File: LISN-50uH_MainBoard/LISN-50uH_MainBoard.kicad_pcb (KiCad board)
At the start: 2 copper layers, 100 x 100 mm, 76 parts, among them J1 Conn_Coaxial, J2 Conn_Coaxial, J3 Conn_01x01_Pin, J4 Conn_01x01_Pin, J5 Conn_01x01_Pin, J6 Conn_01x01_Pin

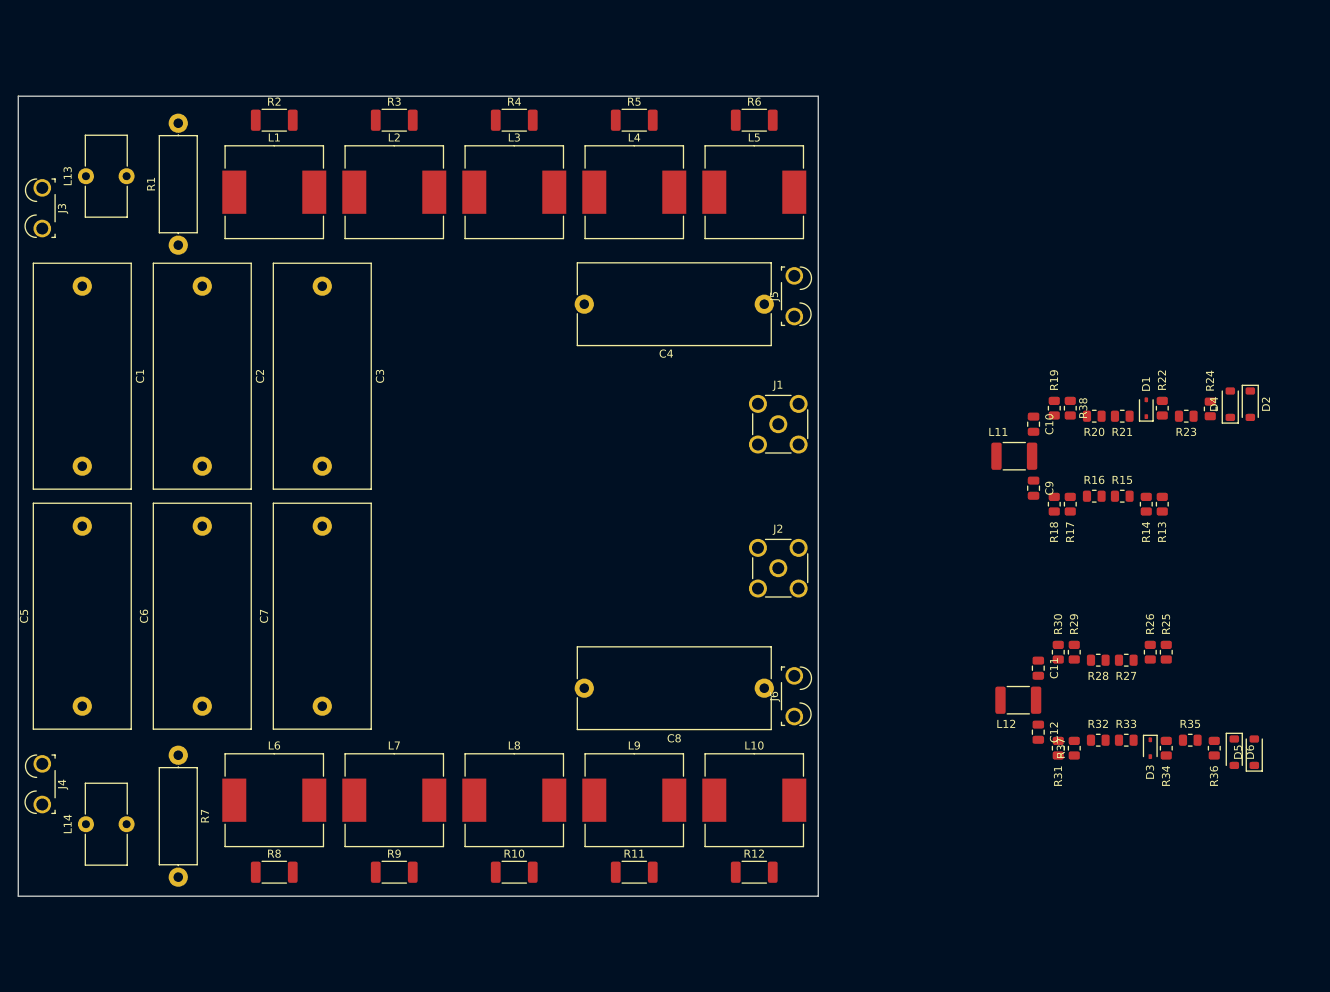
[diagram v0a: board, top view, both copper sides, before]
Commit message: sch update - changes in filter path. pcb - change PCB dimensions
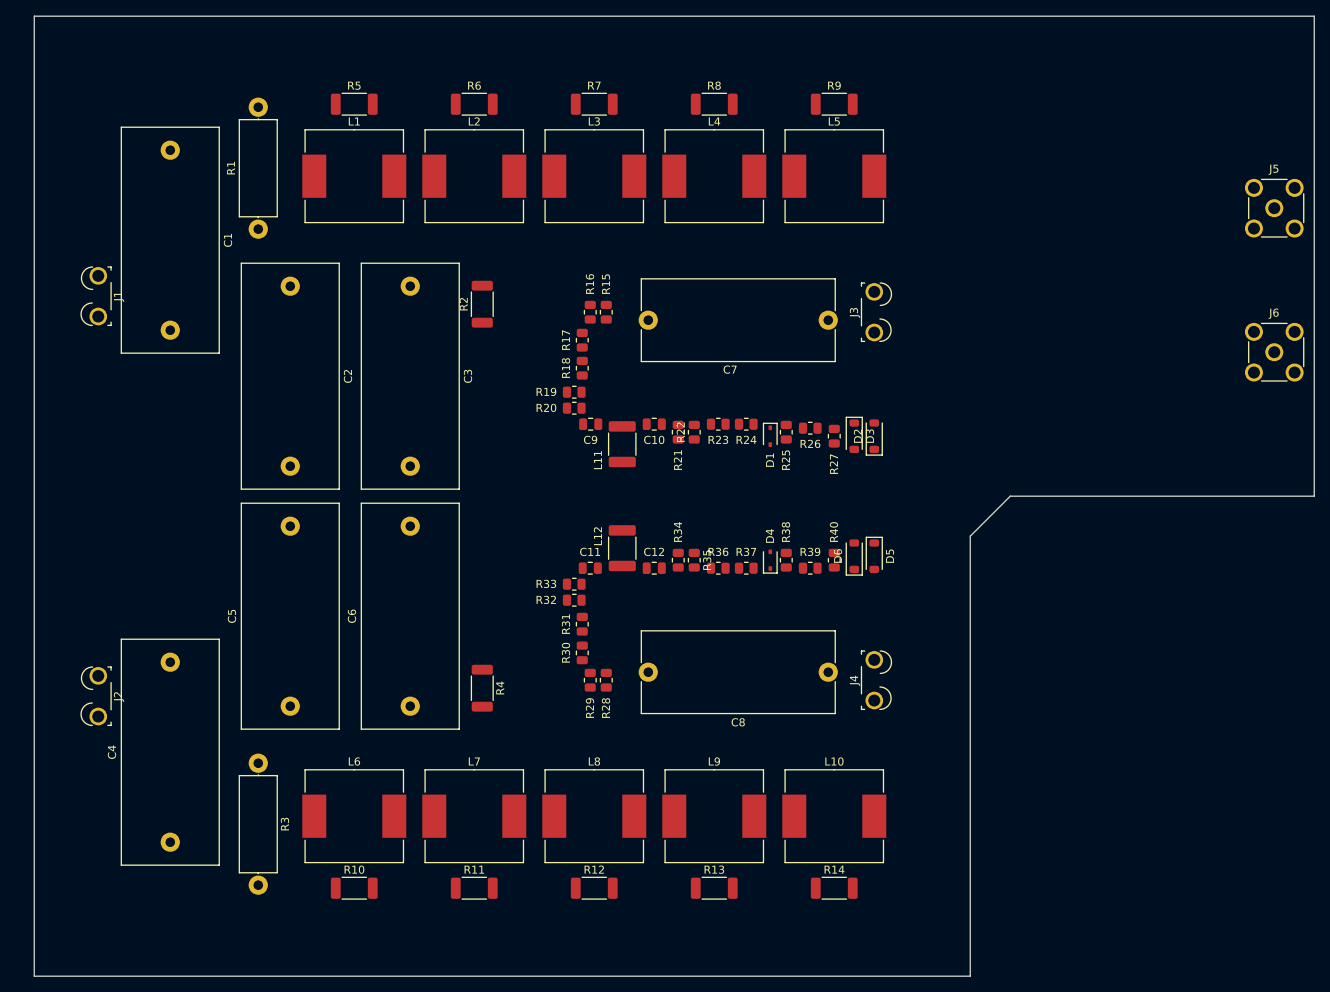
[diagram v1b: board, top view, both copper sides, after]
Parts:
- removed L13, L14: L, Inductor_THT:L_Toroid_Vertical_L10.0mm_W5.0mm_P5.08mm
- added R2: R, Resistor_SMD:R_2010_5025Metric, F.Cu at (126.0, 76.0)
- added R4: R, Resistor_SMD:R_2010_5025Metric, F.Cu at (126.0, 124.0)
- moved R15 73.5 mm to (141.5, 77.0), turned to -90 degrees
- moved R16 73.5 mm to (139.5, 77.0), turned to -90 degrees
- moved R17 70.3 mm to (138.5, 80.5), turned to -90 degrees
- moved R28 70.1 mm to (141.5, 123.0), turned to 90 degrees
- moved R29 70.1 mm to (139.5, 123.0), turned to 90 degrees
- moved R30 68.0 mm to (138.5, 119.6), turned to 90 degrees
- moved J5 67.6 mm to (225.0, 64.0)
- moved J6 67.6 mm to (225.0, 82.0)
- moved R18 66.0 mm to (138.5, 84.0), turned to -90 degrees
- moved R31 64.7 mm to (138.5, 116.0), turned to 90 degrees
- moved R19 63.6 mm to (137.5, 87.0), turned to 0 degrees
- moved R32 62.8 mm to (137.5, 113.0), turned to 0 degrees
- moved R20 61.2 mm to (137.5, 89.0), turned to 0 degrees
- moved R33 61.1 mm to (137.5, 111.0), turned to 0 degrees
- moved C11 57.4 mm to (139.5, 109.0), turned to 0 degrees
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- renumbered C5 to C4, C6 to C5, C7 to C6, C4 to C7, D4 to D3, D3 to D4, J3 to J1, J4 to J2, J5 to J3, J6 to J4, J1 to J5, J2 to J6, R8 to R10, R9 to R11, R10 to R12, R11 to R13, R12 to R14, R13 to R15, R14 to R16, R15 to R17, R16 to R18, R17 to R19, R18 to R20, R19 to R21, R38 to R22, R20 to R23, R21 to R24, R22 to R25, R23 to R26, R24 to R27, R25 to R28, R26 to R29, R7 to R3, R27 to R30, R28 to R31, R29 to R32, R30 to R33, R31 to R34, R37 to R35, R32 to R36, R33 to R37, R34 to R38, R35 to R39, R36 to R40, R2 to R5, R3 to R6, R4 to R7, R5 to R8, R6 to R9
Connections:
- net L_det renamed L_SIG
- net N_det renamed N_SIG
- net Net-(D2-A) renamed L_SIG_LIM
- net Net-(D5-A) renamed N_SIG_LIM
- J1 pad 1: Net-(J3-Pin_1) (its old number) -> Net-(J1-Pin_1)
- J2 pad 1: Net-(J4-Pin_1) (its old number) -> Net-(J2-Pin_1)
- L1 pad 1: Net-(L1-Pad1) -> Net-(J1-Pin_1)
- L6 pad 1: Net-(L14-Pad2) -> Net-(J2-Pin_1)
- R1 pad 2: Net-(L1-Pad1) -> Net-(J1-Pin_1)
- R10 pad 1: Net-(L14-Pad2) -> Net-(J2-Pin_1)
- R3 pad 2: Net-(L14-Pad2) -> Net-(J2-Pin_1)
- R5 pad 1: Net-(L1-Pad1) -> Net-(J1-Pin_1)
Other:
- board size 100 x 100 mm -> 160 x 120 mm

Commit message: changes in low pass filter/limiter path
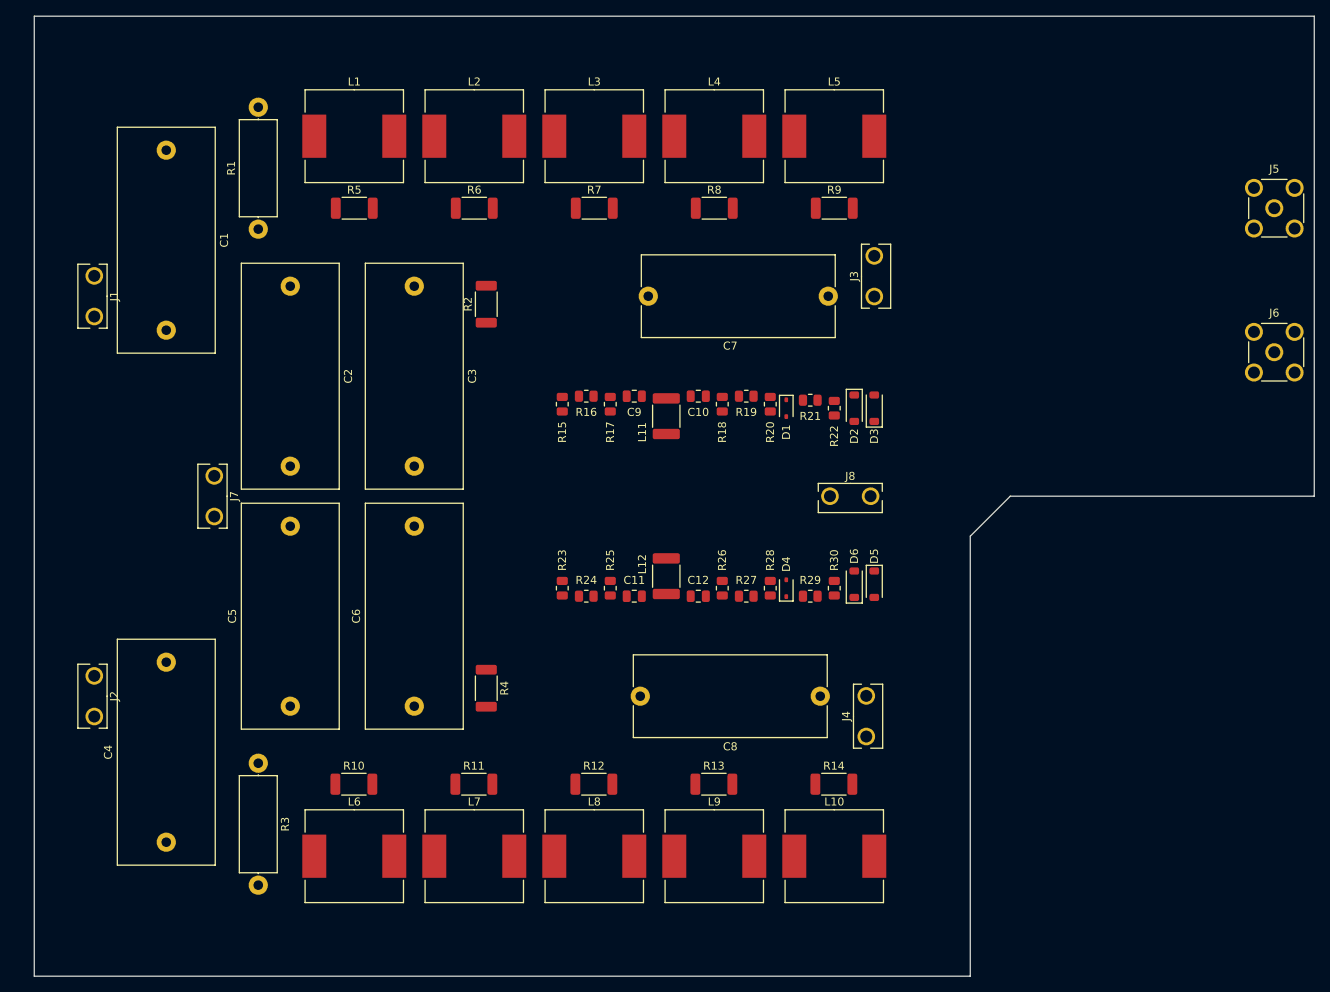
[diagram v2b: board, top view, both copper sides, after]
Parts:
- removed the R16 at (139.5, 77.0)
- removed the R18 at (138.5, 84.0)
- removed the R20 at (137.5, 89.0)
- removed the R22 at (152.5, 92.0)
- removed the R24 at (159.0, 91.0)
- removed the R29 at (139.5, 123.0)
- removed R31: 7R5, Resistor_SMD:R_0805_2012Metric
- removed R33: 430R, Resistor_SMD:R_0805_2012Metric
- removed R35: 220R, Resistor_SMD:R_0805_2012Metric
- removed R37: 15R, Resistor_SMD:R_0805_2012Metric
- added J7: Conn_01x01_Pin, a_project_library:Faston_Tab_6.3x0.8, F.Cu at (92.5, 100.0)
- added J8: Conn_01x01_Pin, a_project_library:Faston_Tab_6.3x0.8, F.Cu at (172.0, 100.0)
- R15: value 620R -> 294R
- R16: renamed from R17; value 10R -> 17R4
- R17: renamed from R19; value 430R -> 215R
- R18: renamed from R21; value 220R -> 110R
- R19: renamed from R23; value 15R -> 30R
- R23: renamed from R28; value 620R -> 294R
- R24: renamed from R30; value 10R -> 17R4
- R25: renamed from R32; value 430R -> 215R
- R26: renamed from R34; value 220R -> 110R
- R27: renamed from R36; value 15R -> 30R
- moved R10 13.0 mm to (110.0, 136.0)
- moved R11 13.0 mm to (125.0, 136.0)
- moved R12 13.0 mm to (139.9, 136.0)
- moved R13 13.0 mm to (154.9, 136.0)
- moved R14 13.0 mm to (169.9, 136.0)
- moved R5 13.0 mm to (110.0, 64.0)
- moved R6 13.0 mm to (125.0, 64.0)
- moved R7 13.0 mm to (140.0, 64.0)
- moved R8 13.0 mm to (155.0, 64.0)
- moved R9 13.0 mm to (170.0, 64.0)
- moved R15 12.7 mm to (136.0, 88.5), turned to 90 degrees
- moved R23 12.7 mm to (136.0, 111.5), turned to -90 degrees
- moved R24 7.11 mm to (139.0, 112.5), turned to 0 degrees
- moved R16 7.02 mm to (139.0, 87.5), turned to 0 degrees
- moved C10 6.52 mm to (153.0, 87.5)
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- renumbered R25 to R20, R26 to R21, R27 to R22, R38 to R28, R39 to R29, R40 to R30
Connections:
- R16 pad 2: Net-(R17-Pad2) -> Net-(C9-Pad1)
- R19 pad 1: Net-(R23-Pad1) -> Net-(D1-A1)
- R24 pad 2: Net-(R30-Pad2) -> Net-(C11-Pad1)
- R27 pad 1: Net-(R36-Pad1) -> Net-(D4-A1)

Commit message: sch - add GDT and optional input toroidal line choke pcb - routing in progress
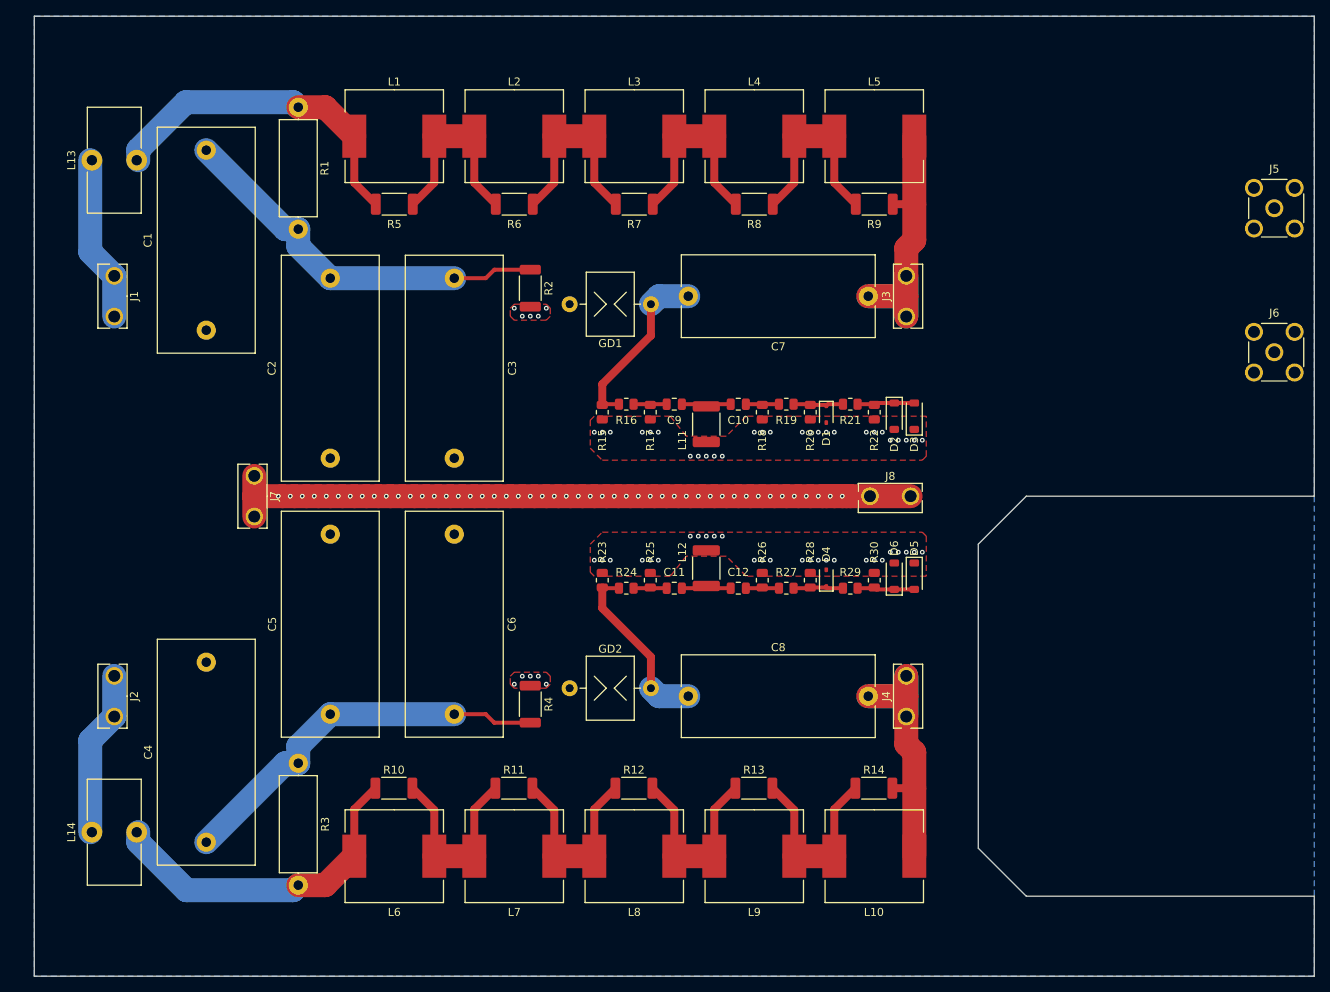
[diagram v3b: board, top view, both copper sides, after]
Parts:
- added GD1: GDT_2Pin, a_project_library:GDT_D8_P10.16_Horizontal, F.Cu at (142.0, 76.0)
- added GD2: GDT_2Pin, a_project_library:GDT_D8_P10.16_Horizontal, F.Cu at (142.0, 124.0)
- added L13: L, Inductor_THT:L_Toroid_Vertical_L13.0mm_W6.5mm_P5.60mm, F.Cu at (77.2, 58.0)
- added L14: L, Inductor_THT:L_Toroid_Vertical_L13.0mm_W6.5mm_P5.60mm, F.Cu at (77.2, 142.0)
- J1, J2, J3, J4, J7, J8: value Conn_01x01_Pin -> Faston Tab 6.3mm
- moved C8 6.00 mm to (174.2, 125.0)
- moved R2 5.85 mm to (132.0, 74.0)
- moved R4 5.85 mm to (132.0, 126.0)
- moved J4 5.59 mm to (179.0, 125.0)
- moved D4 5.15 mm to (169.0, 110.2)
- moved C10 5.10 mm to (158.0, 88.5)
- moved C11 5.10 mm to (150.0, 111.5)
- moved C12 5.10 mm to (158.0, 111.5)
- moved C2 5.10 mm to (107.0, 72.8)
- moved C3 5.10 mm to (122.5, 72.8)
- moved C5 5.10 mm to (107.0, 127.2)
- moved C6 5.10 mm to (122.5, 127.2)
- moved C9 5.10 mm to (150.0, 88.5)
- moved D2 5.10 mm to (180.0, 90.0)
- moved D3 5.10 mm to (177.5, 90.0)
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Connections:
- net Net-(C1-Pad1) renamed /L_C
- net Net-(C4-Pad1) renamed /N_C
- net Net-(J3-Pin_1) renamed /L_dut
- net Net-(J4-Pin_1) renamed /N_dut
- net Net-(L1-Pad2) renamed /L_l1
- net Net-(L10-Pad1) renamed /N_l4
- net Net-(L2-Pad2) renamed /L_l2
- net Net-(L3-Pad2) renamed /L_l3
- net Net-(L4-Pad2) renamed /L_l4
- net Net-(L6-Pad2) renamed /N_l1
- net Net-(L7-Pad2) renamed /N_l2
- net Net-(L8-Pad2) renamed /N_l3
- J1 pad 1: Net-(J1-Pin_1) -> /L_in
- J2 pad 1: Net-(J2-Pin_1) -> /N_in
- L1 pad 1: Net-(J1-Pin_1) -> /L_l
- L6 pad 1: Net-(J2-Pin_1) -> /N_l
- R1 pad 2: Net-(J1-Pin_1) -> /L_l
- R10 pad 1: Net-(J2-Pin_1) -> /N_l
- R3 pad 2: Net-(J2-Pin_1) -> /N_l
- R5 pad 1: Net-(J1-Pin_1) -> /L_l
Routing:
- net GND: track 0.00 -> 87.1 mm, vias 0 -> 112
- net /N_C: track 0.00 -> 48.8 mm
- net /L_C: track 0.00 -> 48.8 mm
- net /L_l: track 0.00 -> 42.1 mm
- net /N_l: track 0.00 -> 42.1 mm
- net /N_dut: track 0.00 -> 40.3 mm
- net /L_dut: track 0.00 -> 40.2 mm
- net /N_l4: track 0.00 -> 24.2 mm
- net /N_l3: track 0.00 -> 24.2 mm
- net /N_l2: track 0.00 -> 24.2 mm
- net /L_l4: track 0.00 -> 24.2 mm
- net /L_l3: track 0.00 -> 24.2 mm
- net /L_l2: track 0.00 -> 24.2 mm
- net /L_l1: track 0.00 -> 24.2 mm
- net /N_l1: track 0.00 -> 24.2 mm
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- added copper zone on B.Cu, net GND
- added copper zone on F.Cu, net GND
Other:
- outline, holes or cut-outs redrawn

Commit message: change input coil footprint, add RF transformer for CM/DM
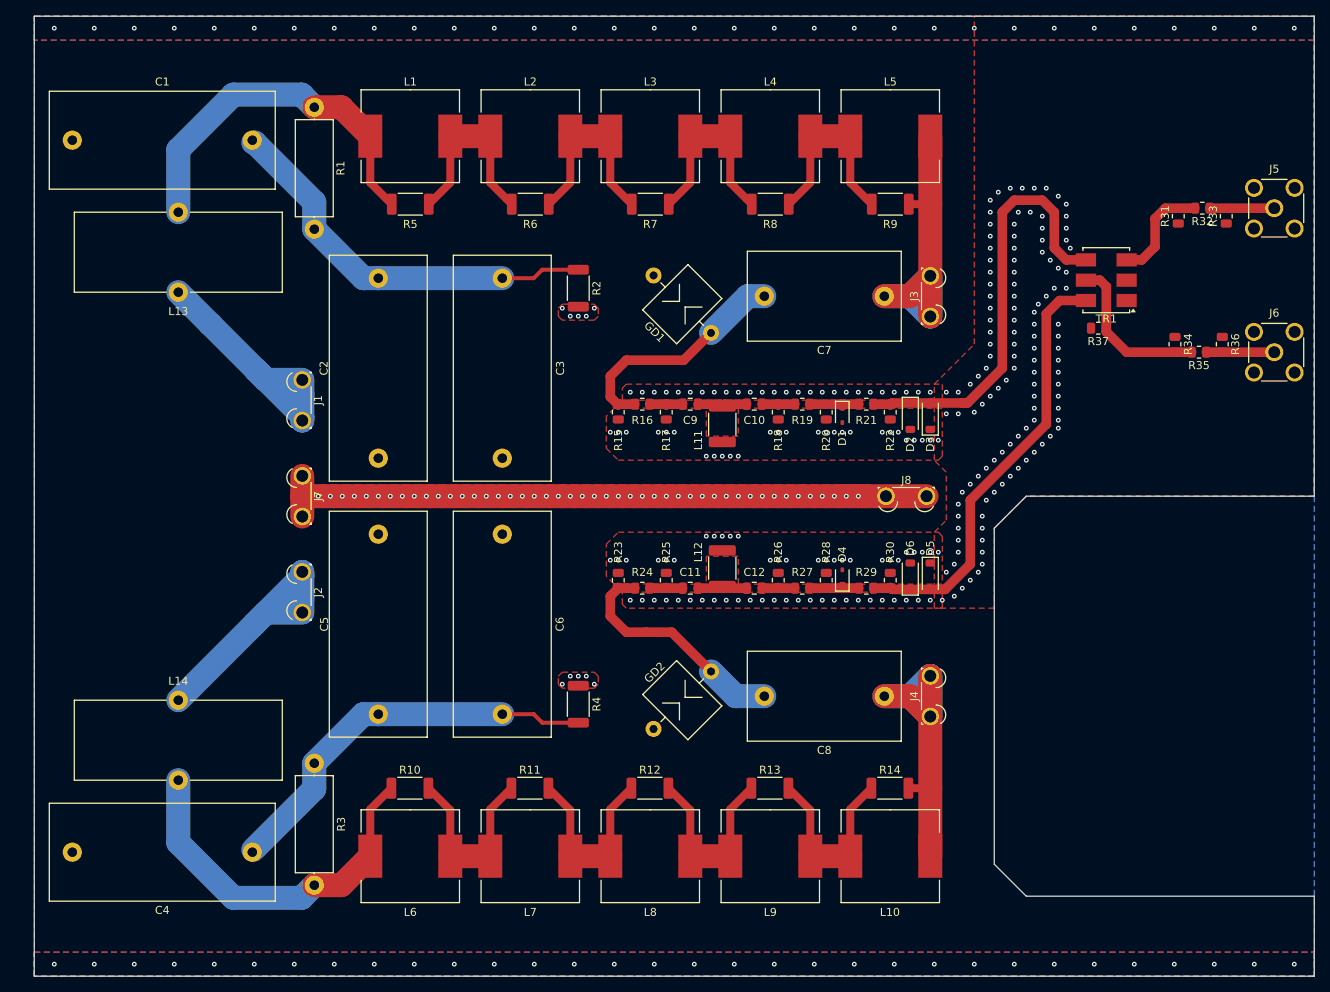
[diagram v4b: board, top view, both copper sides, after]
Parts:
- added R31: DNP, Resistor_SMD:R_0805_2012Metric, F.Cu at (213.0, 65.0)
- added R32: 0, Resistor_SMD:R_0805_2012Metric, F.Cu at (216.0, 64.0)
- added R33: DNP, Resistor_SMD:R_0805_2012Metric, F.Cu at (219.0, 65.0)
- added R34: DNP, Resistor_SMD:R_0805_2012Metric, F.Cu at (212.6, 81.0)
- added R35: 0R, Resistor_SMD:R_0805_2012Metric, F.Cu at (215.6, 82.0)
- added R36: DNP, Resistor_SMD:R_0805_2012Metric, F.Cu at (218.5, 81.0)
- added R37: 50R, Resistor_SMD:R_0805_2012Metric, F.Cu at (203.0, 79.0)
- added TR1: ADT1-6T, RF_Mini-Circuits:Mini-Circuits_CD637_H5.23mm, F.Cu at (204.0, 73.0)
- C7, C8: footprint Capacitor_THT:C_Rect_L24.0mm_W10.1mm_P22.50mm_MKT -> Capacitor_THT:C_Rect_L19.0mm_W11.0mm_P15.00mm_MKS4
- J1, J2, J3, J4, J7, J8: value Faston Tab 6.3mm -> Faston Tab 4.8mm; footprint a_project_library:Faston_Tab_6.3x0.8 -> a_project_library:Faston_Tab_4.8x0.8
- L13, L14: value L -> 250uH optional; footprint Inductor_THT:L_Toroid_Vertical_L13.0mm_W6.5mm_P5.60mm -> a_project_library:L_Toroid_Vertical_L26.0mm_W12.9mm_P10.0mm_Wuerth_WE-FI
- moved J1 26.9 mm to (103.5, 88.0)
- moved J2 26.9 mm to (103.5, 112.0)
- moved L13 15.8 mm to (88.0, 69.5), turned to 180 degrees
- moved L14 15.8 mm to (88.0, 130.5), turned to 0 degrees
- moved GD2 9.12 mm to (151.0, 125.5), turned to 45 degrees
- moved GD1 9.00 mm to (151.0, 76.0), turned to -45 degrees
- moved C2 6.00 mm to (113.0, 72.8)
- moved C3 6.00 mm to (128.5, 72.8)
- moved C5 6.00 mm to (113.0, 127.2)
- moved C6 6.00 mm to (128.5, 127.2)
- moved J7 6.00 mm to (103.5, 100.0)
- moved R2 6.00 mm to (138.0, 74.0)
- moved R4 6.00 mm to (138.0, 126.0)
- moved C1 5.88 mm to (97.2, 55.5), turned to 180 degrees
- moved C4 5.88 mm to (97.2, 144.5), turned to 180 degrees
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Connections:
- J5 pad 1: unconnected-(J5-In-Pad1) -> /SIG_DM_out
- J5 pad 2: unconnected-(J5-Ext-Pad2) -> GND
- J6 pad 1: unconnected-(J6-In-Pad1) -> /SIG_CM_out
- J6 pad 2: unconnected-(J6-Ext-Pad2) -> GND
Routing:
- net N_SIG_LIM: track 7.22 -> 54.4 mm
- net L_SIG_LIM: track 7.22 -> 54.3 mm
- net /SIG_CM: track 0.00 -> 20.3 mm
- net /L_in: track 20.8 -> 34.8 mm
- net /N_in: track 20.8 -> 34.6 mm
- net /SIG_DM: track 0.00 -> 13.3 mm
- net /N_dut: track 40.3 -> 49.1 mm
- net /L_dut: track 40.2 -> 49.0 mm
- net /SIG_CM_out: track 0.00 -> 8.50 mm
- net /SIG_DM_out: track 0.00 -> 8.09 mm
- net N_SIG: track 22.3 -> 29.5 mm
- net L_SIG: track 22.3 -> 29.5 mm
- net GND: track 87.1 -> 82.1 mm, vias 112 -> 344
- net /N_l: track 42.1 -> 46.4 mm
- net /L_l: track 42.1 -> 46.4 mm
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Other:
- outline, holes or cut-outs redrawn
